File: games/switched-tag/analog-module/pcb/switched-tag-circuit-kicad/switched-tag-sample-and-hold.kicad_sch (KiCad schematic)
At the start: 4 parts

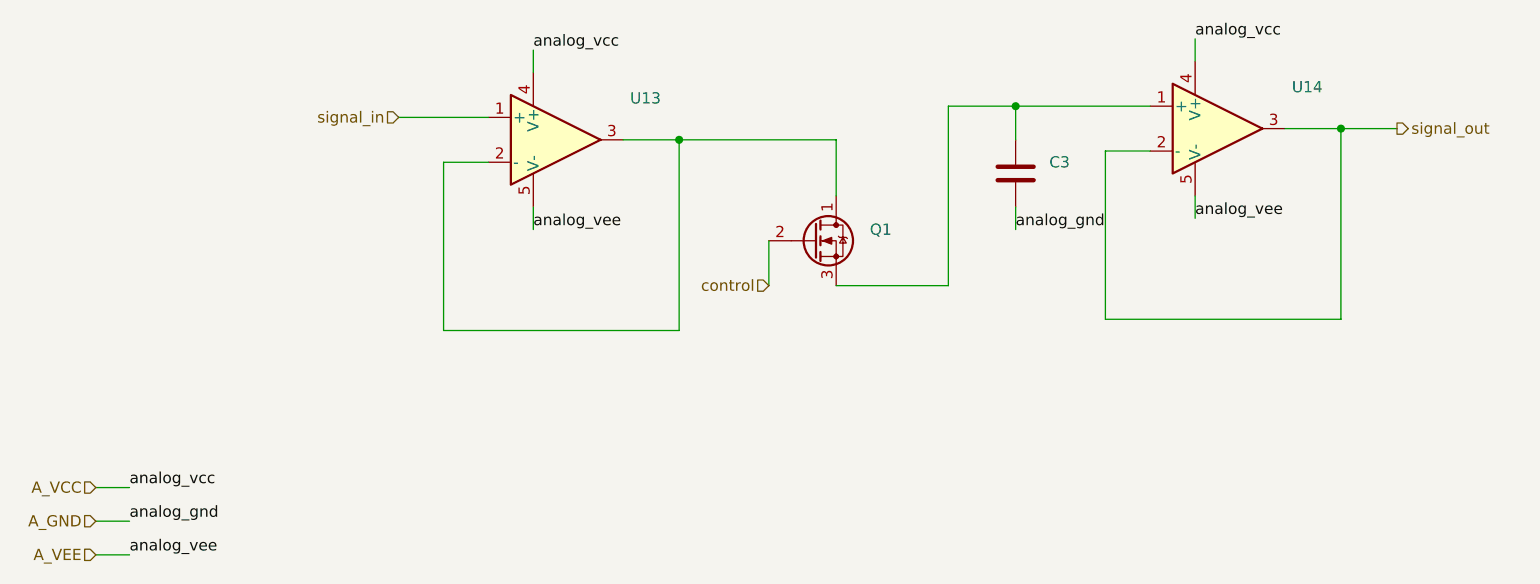
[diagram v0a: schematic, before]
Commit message: Converted Lm358.mod to .lib file for convenience.
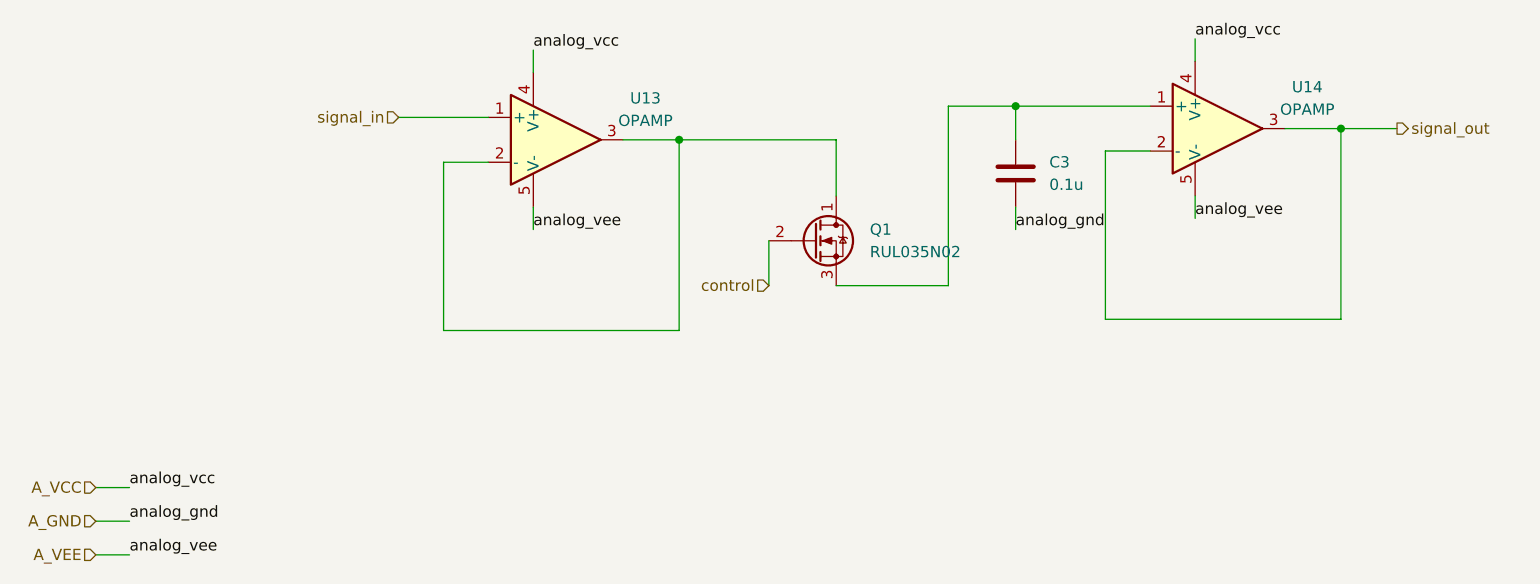
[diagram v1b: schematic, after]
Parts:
- C3: value (none) -> 0.1u
- Q1: value (none) -> RUL035N02; Spice_Lib_File ../../../../../spice-models/rul035n02.lib -> (none); Spice_Model RUL035N02 -> (none); Spice_Netlist_Enabled Y -> (none); Spice_Primitive X -> (none)
- U13, U14: value (none) -> OPAMP; Spice_Lib_File /home/pab/Inventions/analog-circuit-game-console/ms-circuit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 -> (none); Spice_Model AD8031 -> (none); Spice_Netlist_Enabled Y -> (none); Spice_Node_Sequence 1 2 4 5 3 -> (none); Spice_Primitive X -> (none)
